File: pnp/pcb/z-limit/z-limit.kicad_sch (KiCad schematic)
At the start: 3 parts, among them J1 AUX, J2 HEAD_HARNESS, SW1 SW_SPDT

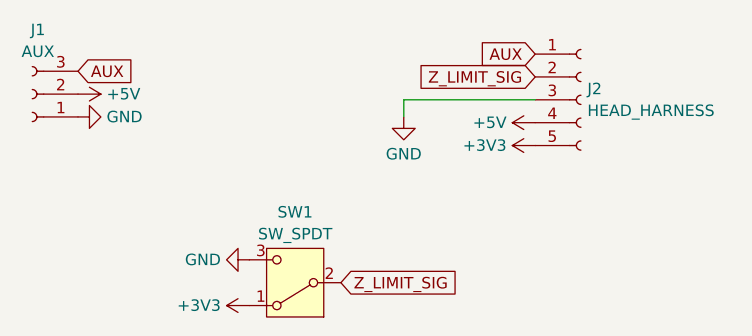
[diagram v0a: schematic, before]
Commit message: updates zlimit to rev00b2 with fixed switch pinout
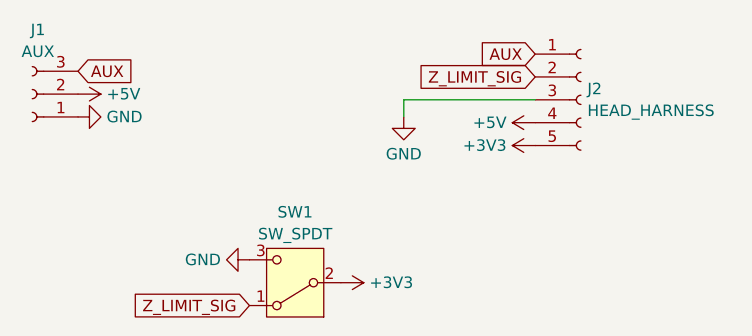
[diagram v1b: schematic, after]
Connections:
- net +3V3: now also SW1.2 (B); no longer SW1.1 (A)
- net Z_LIMIT_SIG: now also SW1.1 (A); no longer SW1.2 (B)
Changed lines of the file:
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@@
     (stroke (width 0) (type default))
   )
-  (global_label "Z_LIMIT_SIG" (shape input) (at 165.1 71.12 0) (fields_autoplaced)
-    (effects (font (size 1.27 1.27)) (justify left))
-    (property "Intersheetrefs" "${INTERSHEET_REFS}" (at 178.9709 71.12 0)
-      (effects (font (size 1.27 1.27)) (justify left) hide)
+  (global_label "Z_LIMIT_SIG" (shape input) (at 154.94 73.66 180) (fields_autoplaced)
+    (effects (font (size 1.27 1.27)) (justify right))
+    (property "Intersheetrefs" "${INTERSHEET_REFS}" (at 141.0691 73.66 0)
+      (effects (font (size 1.27 1.27)) (justify right) hide)
     )
   )
@@
     )
   )
-  (symbol (lib_id "power:+3V3") (at 154.94 73.66 90) (unit 1)
+  (symbol (lib_id "power:+3V3") (at 165.1 71.12 270) (unit 1)
     (in_bom yes) (on_board yes) (dnp no) (fields_autoplaced)
-    (property "Reference" "#PWR06" (at 158.75 73.66 0)
+    (property "Reference" "#PWR06" (at 161.29 71.12 0)
       (effects (font (size 1.27 1.27)) hide)
     )
-    (property "Value" "+3V3" (at 151.765 73.66 90)
+    (property "Value" "+3V3" (at 168.275 71.12 90)
       (effects (font (size 1.27 1.27)) (justify left))
     )
-    (property "Footprint" "" (at 154.94 73.66 0)
+    (property "Footprint" "" (at 165.1 71.12 0)
       (effects (font (size 1.27 1.27)) hide)
     )
-    (property "Datasheet" "" (at 154.94 73.66 0)
+    (property "Datasheet" "" (at 165.1 71.12 0)
       (effects (font (size 1.27 1.27)) hide)
     )

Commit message: updates with all current v4 pcbs
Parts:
- J1: LCSC Part Number (none) -> C157929; MFG Part Number (none) -> S3B-PH-K-S(LF)(SN)
- J2: LCSC Part Number (none) -> C2845454; MFG Part Number (none) -> HC-PH-5ALT
- SW1: LCSC Part Number (none) -> C466018; MFG Part Number (none) -> DM1-12UC-1
